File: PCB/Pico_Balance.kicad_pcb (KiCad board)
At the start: 2 copper layers, 100 x 52 mm, 42 parts, among them J1 XT60PW-M, J2 GPIO_Ext, J3 Conn_Motor0, J4 Conn_Motor1, J5 5V3A OUT, Q1 CSD17577Q3A, U1 BMI323, U2 DRV8876PWPR, U3 DRV8876PWPR, U4 LM74610QDGKRQ1, U5 LMR51430

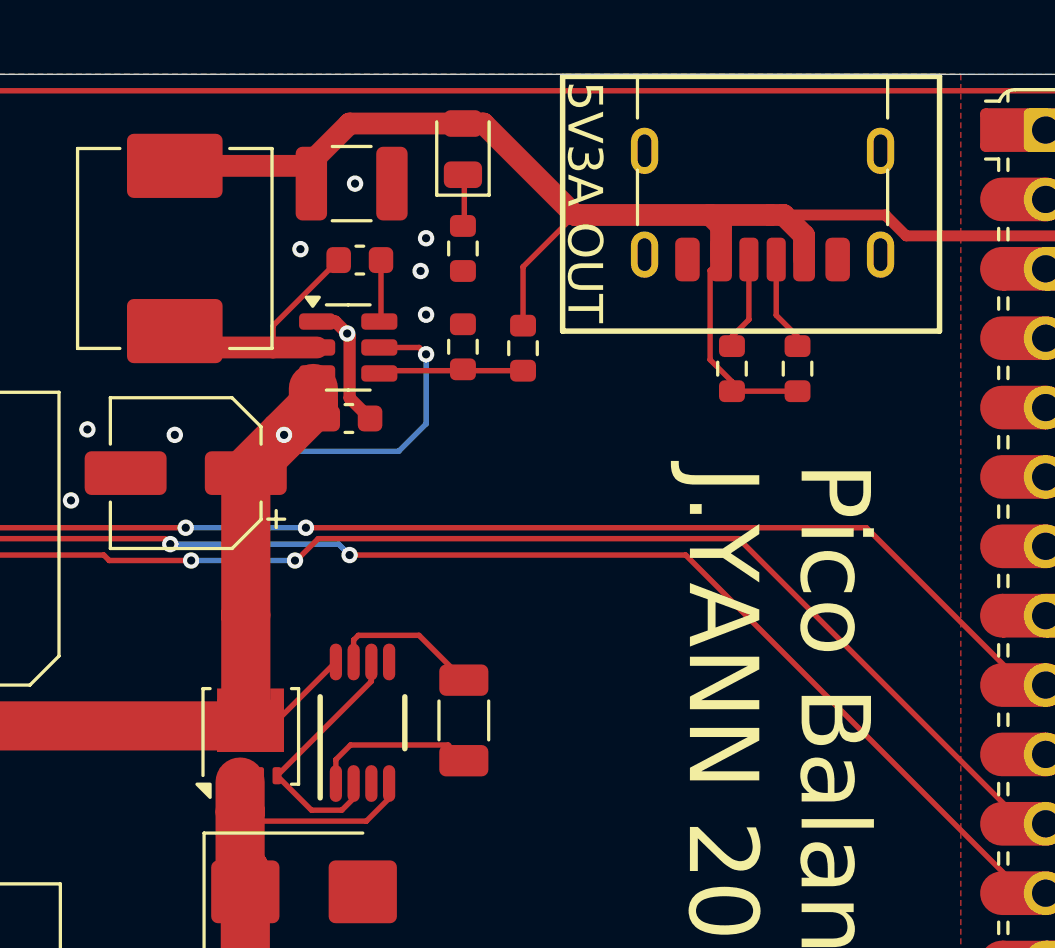
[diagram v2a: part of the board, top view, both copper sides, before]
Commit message: improve routing around switching regulator
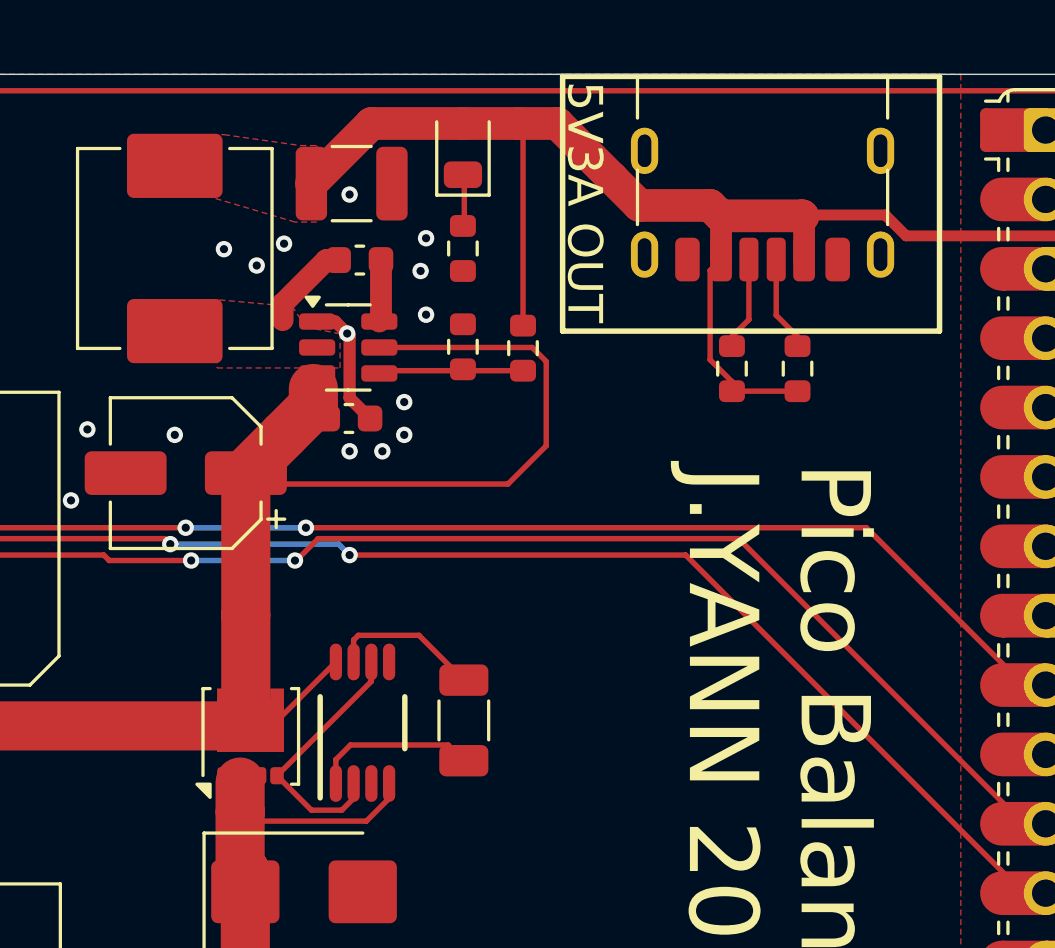
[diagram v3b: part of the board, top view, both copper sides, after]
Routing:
- net VM: track 85.5 -> 96.7 mm, vias 2 -> 0
- net /SW: track 9.66 -> 3.31 mm
- net +5V: track 116.1 -> 113.2 mm
- net GND: vias 17 -> 23
- added copper zone on F.Cu, net +5V
- added copper zone on F.Cu, net /SW

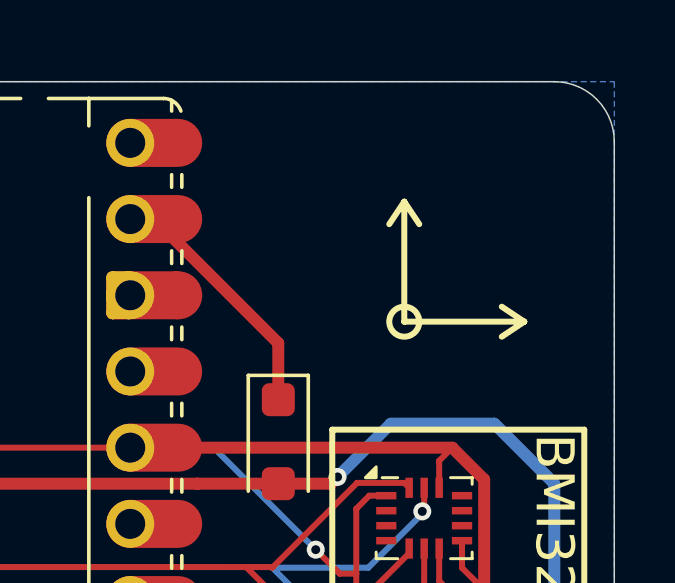
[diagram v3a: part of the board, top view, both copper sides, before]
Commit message: Minor Silkscreen Adjustments
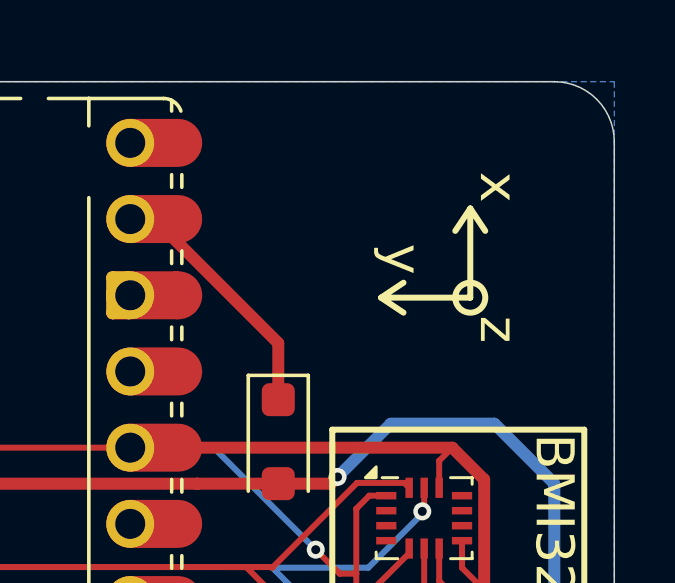
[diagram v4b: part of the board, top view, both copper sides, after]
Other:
- board text added: "x"
- board text added: "y"
- board text added: "z"
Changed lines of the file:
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@@
 	)
 	(gr_line
-		(start 249 80)
-		(end 248.25 80.5)
+		(start 247.2 76.225)
+		(end 247.7 76.975)
 		(stroke
 			(width 0.2)
@@
 	)
 	(gr_line
-		(start 245 80)
-		(end 249 80)
+		(start 247.2 79.2)
+		(end 247.2 76.4)
 		(stroke
 			(width 0.2)
@@
 	)
 	(gr_line
-		(start 249 80)
-		(end 248.25 79.5)
+		(start 247.2 76.225)
+		(end 246.7 76.975)
 		(stroke
 			(width 0.2)
@@
 	)
 	(gr_line
-		(start 245 76)
-		(end 245.5 76.75)
+		(start 244.225 79.2)
+		(end 244.975 78.7)
 		(stroke
 			(width 0.2)
@@
 	)
 	(gr_circle
-		(center 245 80)
-		(end 245.5 80)
+		(center 247.2 79.2)
+		(end 247.2 78.7)
 		(stroke
 			(width 0.2)
@@
 	)
 	(gr_line
-		(start 245 76)
-		(end 244.5 76.75)
+		(start 244.225 79.2)
+		(end 244.975 79.7)
 		(stroke
 			(width 0.2)
@@
 	)
 	(gr_line
-		(start 245 80)
-		(end 245 76)
+		(start 247.2 79.2)
+		(end 244.4 79.2)
 		(stroke
 			(width 0.2)
@@
 		)
 	)
+	(gr_text "y"
+		(at 244.2 77.4 270)
+		(layer "F.SilkS")
+		(effects
+			(font
+				(size 1.27 1.27)
+				(thickness 0.2)
+			)
+			(justify left bottom)
+		)
+	)
 	(gr_text "MOTOR 1"
 		(at 173 114.4 270)
@@
 		)
 	)
+	(gr_text "x"
+		(at 247.4 75 270)
+		(layer "F.SilkS")
+		(effects
+			(font
+				(size 1.27 1.27)
+				(thickness 0.2)
+			)
+			(justify left bottom)
+		)
+	)
 	(gr_text "MOTOR 0"
 		(at 173 72.8 270)
@@
 		)
 	)
+	(gr_text "z"
+		(at 247.4 79.8 270)
+		(layer "F.SilkS")
+		(effects
+			(font
+				(size 1.27 1.27)
+				(thickness 0.2)
+			)
+			(justify left bottom)
+		)
+	)
 	(table
 		(column_count 1)
@@
 		(cells
 			(table_cell "M+"
-				(start 171.95 73.725)
-				(end 169.3 77.275)
+				(start 171.975 118.725)
+				(end 169.325 122.275)
 				(margins 0.1 0.1 0.1 0.1)
 				(span 1 1)
@@
 			)
 			(table_cell "3V"
-				(start 169.3 73.725)
-				(end 166.8 77.275)
+				(start 169.325 118.725)
+				(end 166.825 122.275)
 				(margins 0.1 0.1 0.1 0.1)
 				(span 1 1)
@@
 			)
 			(table_cell "EA"
-				(start 166.8 73.725)
-				(end 164.4 77.275)
+				(start 166.825 118.725)
+				(end 164.425 122.275)
 				(margins 0.1 0.1 0.1 0.1)
 				(span 1 1)
@@
 			)
 			(table_cell "EB"
-				(start 164.4 73.725)
-				(end 161.6 77.275)
+				(start 164.425 118.725)
+				(end 161.625 122.275)
 				(margins 0.1 0.1 0.1 0.1)
 				(span 1 1)
@@
 			)
 			(table_cell "GND"
-				(start 161.6 73.725)
-				(end 159.4 77.275)
+				(start 161.625 118.725)
+				(end 159.425 122.275)
 				(margins 0.1 0.1 0.1 0.1)
 				(span 1 1)
@@
 			)
 			(table_cell "M-"
-				(start 159.4 73.725)
-				(end 156.8 77.275)
+				(start 159.425 118.725)
+				(end 156.825 122.275)
 				(margins 0.1 0.1 0.1 0.1)
 				(span 1 1)
@@
 		(cells
 			(table_cell "M+"
-				(start 171.975 118.725)
-				(end 169.325 122.275)
+				(start 171.95 73.725)
+				(end 169.3 77.275)
 				(margins 0.1 0.1 0.1 0.1)
 				(span 1 1)
@@
 			)
 			(table_cell "3V"
-				(start 169.325 118.725)
-				(end 166.825 122.275)
+				(start 169.3 73.725)
+				(end 166.8 77.275)
 				(margins 0.1 0.1 0.1 0.1)
 				(span 1 1)
@@
 			)
 			(table_cell "EA"
-				(start 166.825 118.725)
-				(end 164.425 122.275)
+				(start 166.8 73.725)
+				(end 164.4 77.275)
 				(margins 0.1 0.1 0.1 0.1)
 				(span 1 1)
@@
 			)
 			(table_cell "EB"
-				(start 164.425 118.725)
-				(end 161.625 122.275)
+				(start 164.4 73.725)
+				(end 161.6 77.275)
 				(margins 0.1 0.1 0.1 0.1)
 				(span 1 1)
@@
 			)
 			(table_cell "GND"
-				(start 161.625 118.725)
-				(end 159.425 122.275)
+				(start 161.6 73.725)
+				(end 159.4 77.275)
 				(margins 0.1 0.1 0.1 0.1)
 				(span 1 1)
@@
 			)
 			(table_cell "M-"
-				(start 159.425 118.725)
-				(end 156.825 122.275)
+				(start 159.4 73.725)
+				(end 156.8 77.275)
 				(margins 0.1 0.1 0.1 0.1)
 				(span 1 1)
@@
 	)
 	(group ""
-		(members "0e098a54-aab8-48f0-ad5a-1b8c5dcb6939" "3d4db691-04d1-4923-84a8-ca63cf973a07"
-			"4c652e14-a829-45d9-ae98-6ccd60f11574" "63e503f4-efba-4b57-b139-408cbbdc4a5a"
-			"90350472-ea7e-46d9-adf6-18d1887b5930" "97e5d2a3-c56d-46de-99b1-c52cc26e95a4"
-			"af4be8ed-c6e8-495a-9d4b-11de16a7dfe8"
-		)
-	)
-	(group ""
